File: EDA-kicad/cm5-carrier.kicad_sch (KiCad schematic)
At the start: 6 parts

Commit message: set everything except from power to DNP
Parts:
- C1, C2, C3, C4, Module1, R1: now not fitted

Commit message: setup layers
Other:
- note added: "POWER SECTION labels"

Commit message: minor pcb progress
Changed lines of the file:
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@@
 	(text "POWER SECTION labels\n"
 		(exclude_from_sim no)
-		(at 342.138 173.482 0)
+		(at 335.788 146.558 0)
 		(effects
 			(font

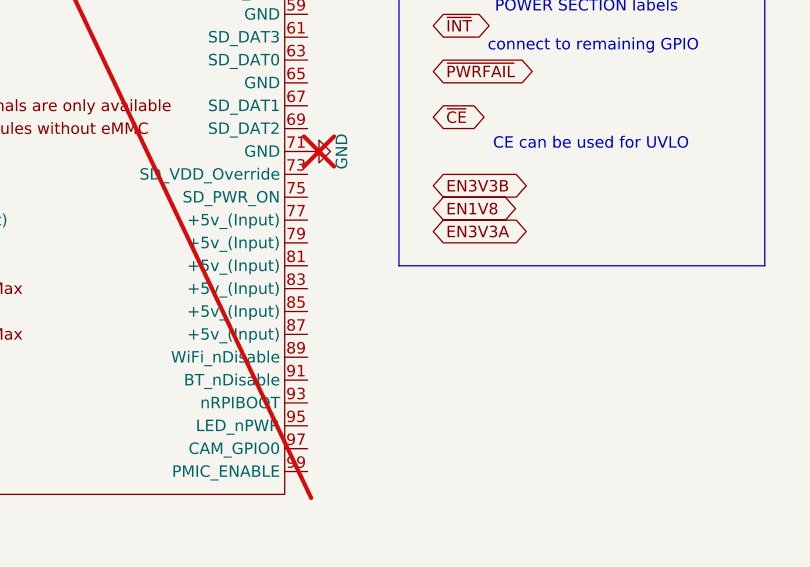
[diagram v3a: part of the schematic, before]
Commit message: connect CM5 to 5V 6A rail
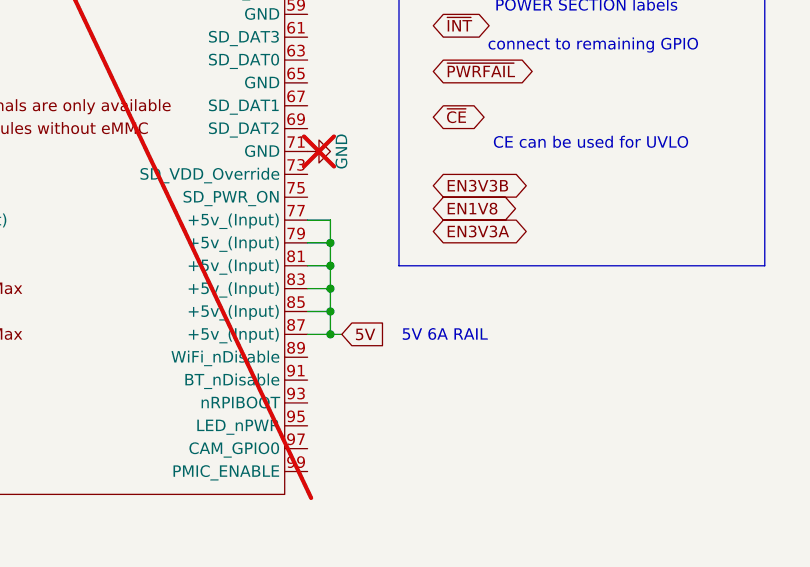
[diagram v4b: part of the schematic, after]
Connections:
- net 5V: now reaches Module1.77 (+5v_(Input))
- net 5V: now also Module1.79 (+5v_(Input)), Module1.81 (+5v_(Input)), Module1.83 (+5v_(Input)), Module1.85 (+5v_(Input)), Module1.87 (+5v_(Input))
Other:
- note added: "5V 6A RAIL"

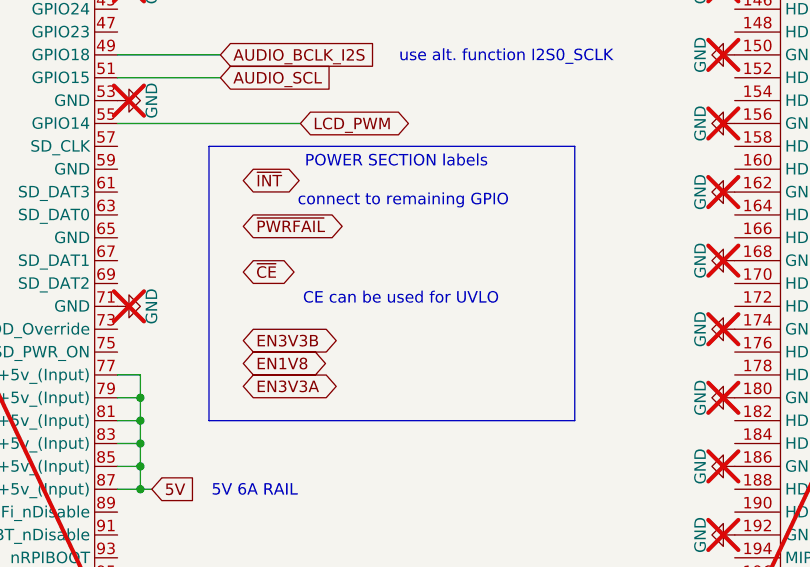
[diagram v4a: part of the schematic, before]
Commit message: distinguish between BQ INT and TPS INT pins
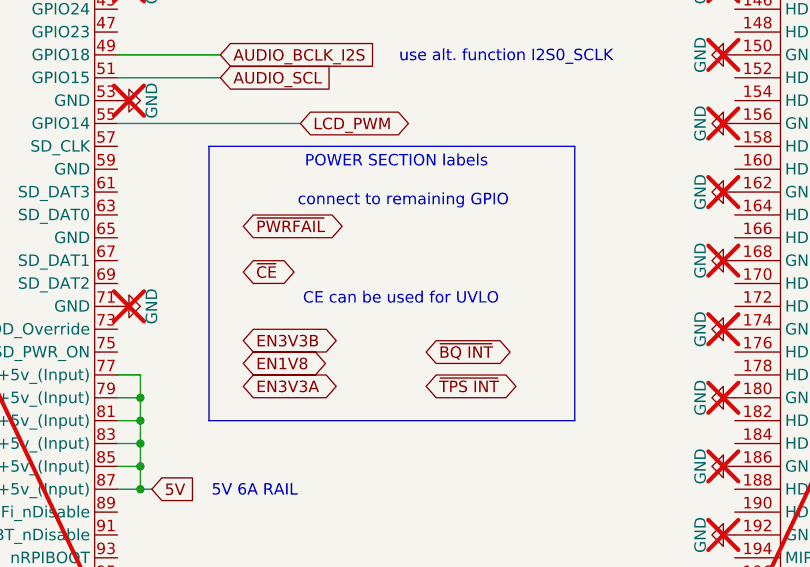
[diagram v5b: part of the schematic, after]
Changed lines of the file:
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@@
 		)
 	)
-	(global_label "~{INT}"
-		(shape bidirectional)
-		(at 318.77 148.59 0)
-		(fields_autoplaced yes)
-		(effects
-			(font
-				(size 1.27 1.27)
-			)
-			(justify left)
-		)
-		(property "Intersheetrefs" "${INTERSHEET_REFS}"
-			(at 325.7694 148.59 0)
+	(global_label "~{TPS INT}"
+		(shape bidirectional)
+		(at 339.09 171.45 0)
+		(fields_autoplaced yes)
+		(effects
+			(font
+				(size 1.27 1.27)
+			)
+			(justify left)
+		)
+		(property "Intersheetrefs" "${INTERSHEET_REFS}"
+			(at 350.5041 171.45 0)
 			(effects
 				(font
@@
 			(effects
 				(font
+					(size 1.27 1.27)
+				)
+				(justify left)
+				(hide yes)
+			)
+		)
+	)
+	(global_label "~{BQ INT}"
+		(shape bidirectional)
+		(at 339.09 167.64 0)
+		(fields_autoplaced yes)
+		(effects
+			(font
+				(size 1.27 1.27)
+			)
+			(justify left)
+		)
+		(property "Intersheetrefs" "${INTERSHEET_REFS}"
+			(at 349.6575 167.64 0)
+			(effects
+				(font

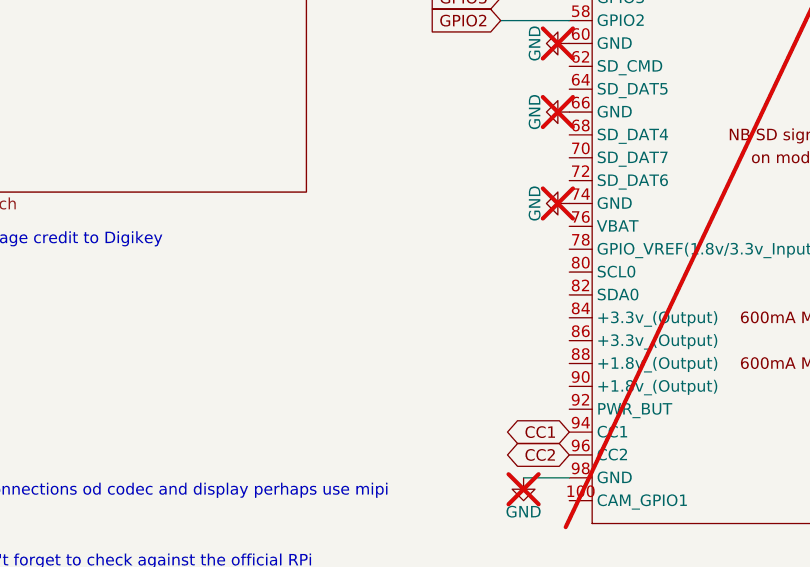
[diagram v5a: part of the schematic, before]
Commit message: connect PMIC I2C to CM5
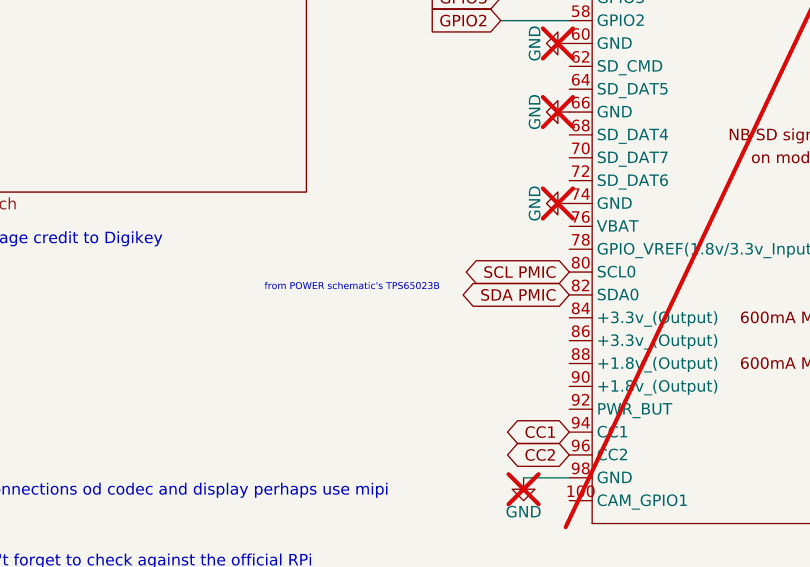
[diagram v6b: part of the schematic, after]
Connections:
- net SCL PMIC: now reaches Module1.80 (SCL0)
- net SDA PMIC: now reaches Module1.82 (SDA0)
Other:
- note added: "from POWER schematic's TPS65023B"
